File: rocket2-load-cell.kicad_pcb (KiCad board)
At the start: 2 copper layers, 45.1 x 100.6 mm, 41 parts, among them J1 SWD, J2 Screw_Terminal_01x02, J3 629105150521, U1 STM32F103C8Tx, U2 AMS1117-3.3, Y1 16MHz

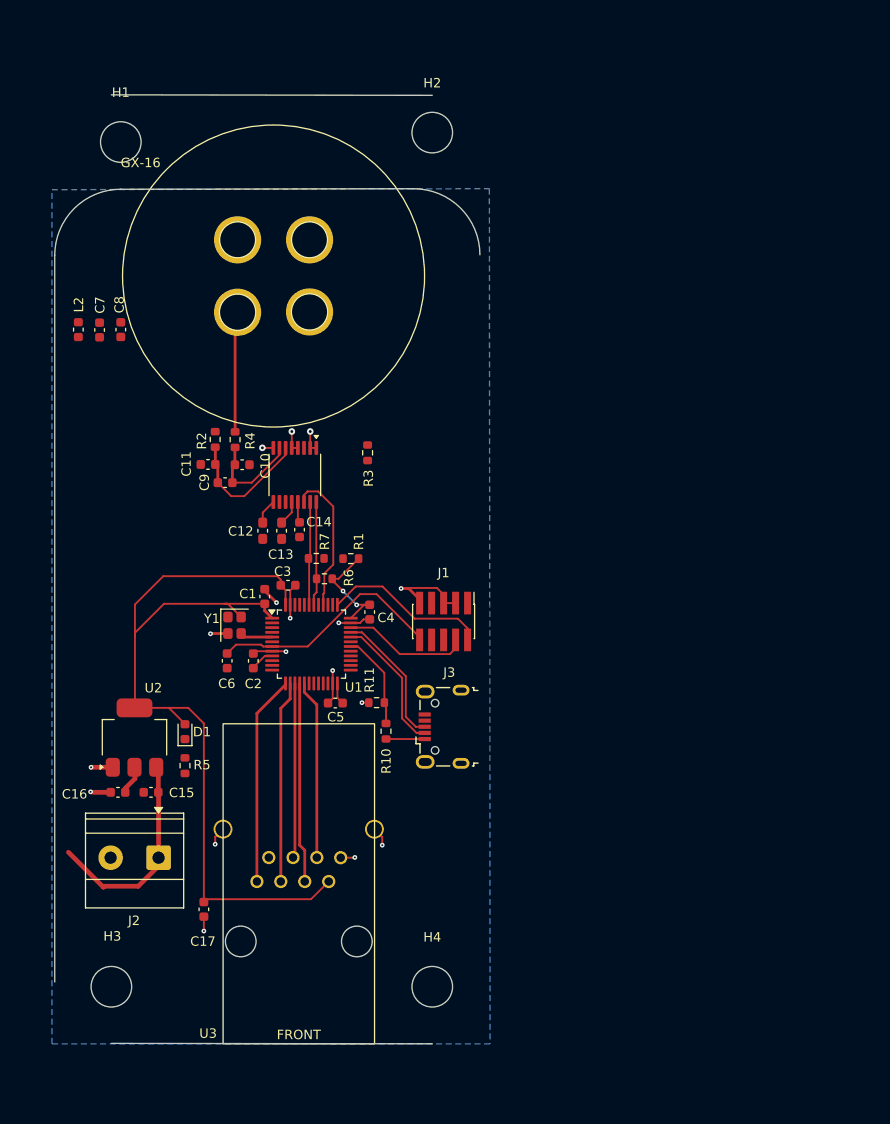
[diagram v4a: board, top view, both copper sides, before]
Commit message: complete power + signal routing
fixed bends, shortened length from MCU -> ADC -> Load Cell
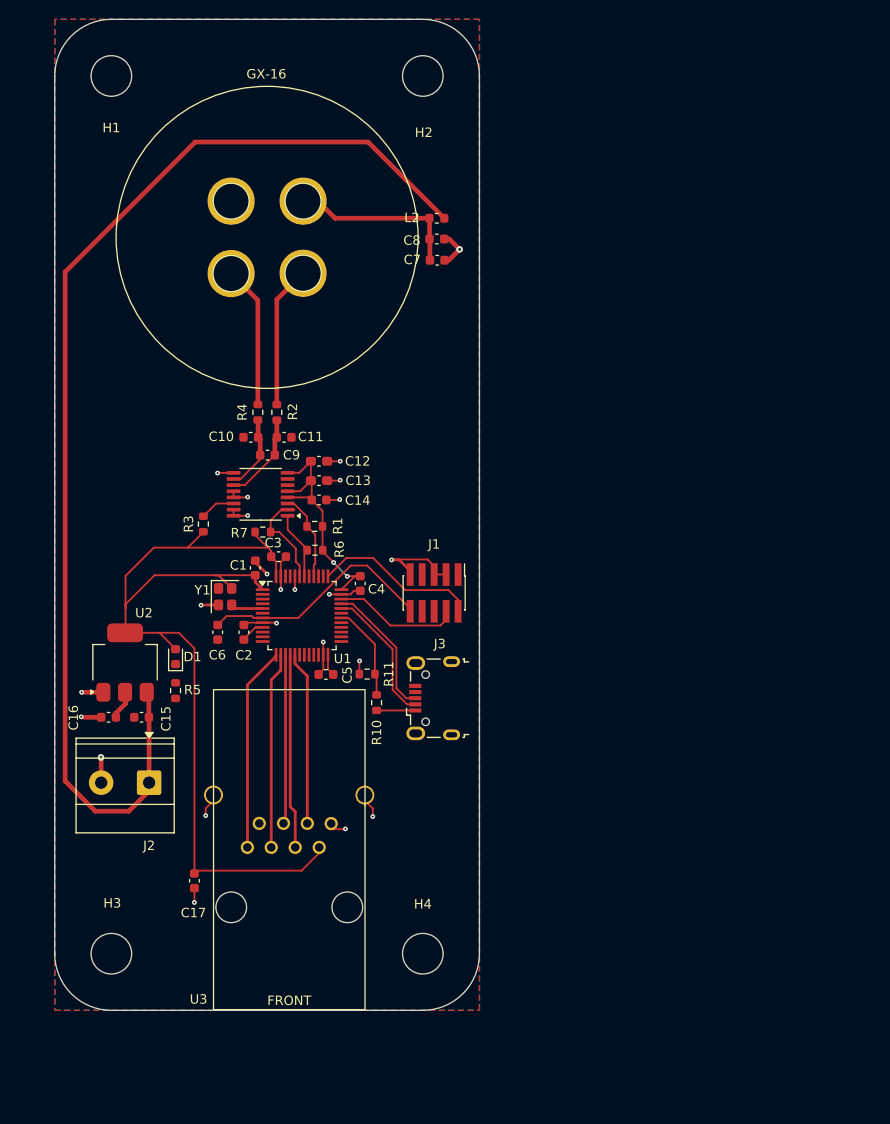
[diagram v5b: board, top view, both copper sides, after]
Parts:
- moved L2 39.8 mm to (150.5, 56.1), turned to 0 degrees
- moved C7 36.5 mm to (150.5, 60.5), turned to 0 degrees
- moved C8 34.8 mm to (150.5, 58.3), turned to 0 degrees
- moved R3 19.0 mm to (125.8, 88.5)
- moved C12 9.48 mm to (138.0, 81.8), turned to 0 degrees
- moved C11 8.57 mm to (134.3, 79.3), turned to 180 degrees
- moved C15 8.01 mm to (119.2, 109.0)
- moved C16 8.01 mm to (115.7, 109.0)
- moved J2 8.01 mm to (120.0, 115.9)
- moved R5 8.01 mm to (122.8, 106.1)
- moved D1 8.01 mm to (122.8, 102.5)
- moved U2 8.01 mm to (117.5, 103.2)
- moved R2 7.13 mm to (133.5, 76.6)
- moved H1 7.07 mm to (116.0, 41.0)
- moved C13 6.63 mm to (138.0, 83.9), turned to 0 degrees
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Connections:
- ADS1219 pad 1: GND -> ADS_CLK
- ADS1219 pad 10: unconnected-(ADS1219-AIN1-Pad10) -> Net-(ADS1219-AIN1)
- ADS1219 pad 11: unconnected-(ADS1219-AIN0-Pad11) -> Net-(ADS1219-AIN0)
- ADS1219 pad 12: +3.3V -> GND
- ADS1219 pad 13: +3.3V -> GND
- ADS1219 pad 14: ADS_DRDY -> Net-(ADS1219-DRDY)
- ADS1219 pad 15: ADS_DATA -> GND
- ADS1219 pad 16: ADS_CLK -> GND
- ADS1219 pad 2: GND -> ADS_DATA
- ADS1219 pad 3: Net-(ADS1219-RESET) -> ADS_DRDY
- ADS1219 pad 4: GND -> +3.3V
- ADS1219 pad 5: GND -> +3.3V
- ADS1219 pad 6: Net-(ADS1219-AIN3) -> unconnected-(ADS1219-AIN3-Pad6)
- ADS1219 pad 7: Net-(ADS1219-AIN2) -> unconnected-(ADS1219-AIN2-Pad7)
- ADS1219 pad 8: GND -> +3.3V
- ADS1219 pad 9: +3.3V -> GND
- C10 pad 2: Net-(ADS1219-AIN2) -> Net-(ADS1219-AIN1)
- C11 pad 2: Net-(ADS1219-AIN3) -> Net-(ADS1219-AIN0)
- C9 pad 1: Net-(ADS1219-AIN3) -> Net-(ADS1219-AIN0)
- C9 pad 2: Net-(ADS1219-AIN2) -> Net-(ADS1219-AIN1)
- R2 pad 2: Net-(ADS1219-AIN3) -> Net-(ADS1219-AIN0)
- R3 pad 1: Net-(ADS1219-RESET) -> Net-(ADS1219-DRDY)
- R4 pad 2: Net-(ADS1219-AIN2) -> Net-(ADS1219-AIN1)
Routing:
- net VBUS: track 22.6 -> 124.8 mm
- net VLC: track 0.00 -> 18.6 mm
- net AIN-: track 0.00 -> 15.1 mm
- net Net-(ADS1219-AIN3): track 14.2 -> 0.00 mm
- net GND: track 47.0 -> 60.6 mm, vias 17 -> 23
- net +3.3V: track 120.9 -> 132.8 mm
- net Net-(ADS1219-AIN2): track 10.8 -> 0.00 mm
- net Net-(ADS1219-AIN0): track 0.00 -> 9.80 mm
- net Net-(ADS1219-AIN1): track 0.00 -> 7.94 mm
- net ADS_DRDY: track 15.5 -> 9.37 mm
- net Net-(ADS1219-DRDY): track 0.00 -> 3.76 mm
- net ADS_CLK: track 11.0 -> 7.33 mm
- net AIN+: track 12.8 -> 15.0 mm
- net ETH_RX: track 21.2 -> 20.6 mm
- net ETH_RTS: track 21.4 -> 20.8 mm
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- added copper zone on F.Cu, net GND
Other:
- board size 45.1 x 100.6 mm -> 45 x 105 mm

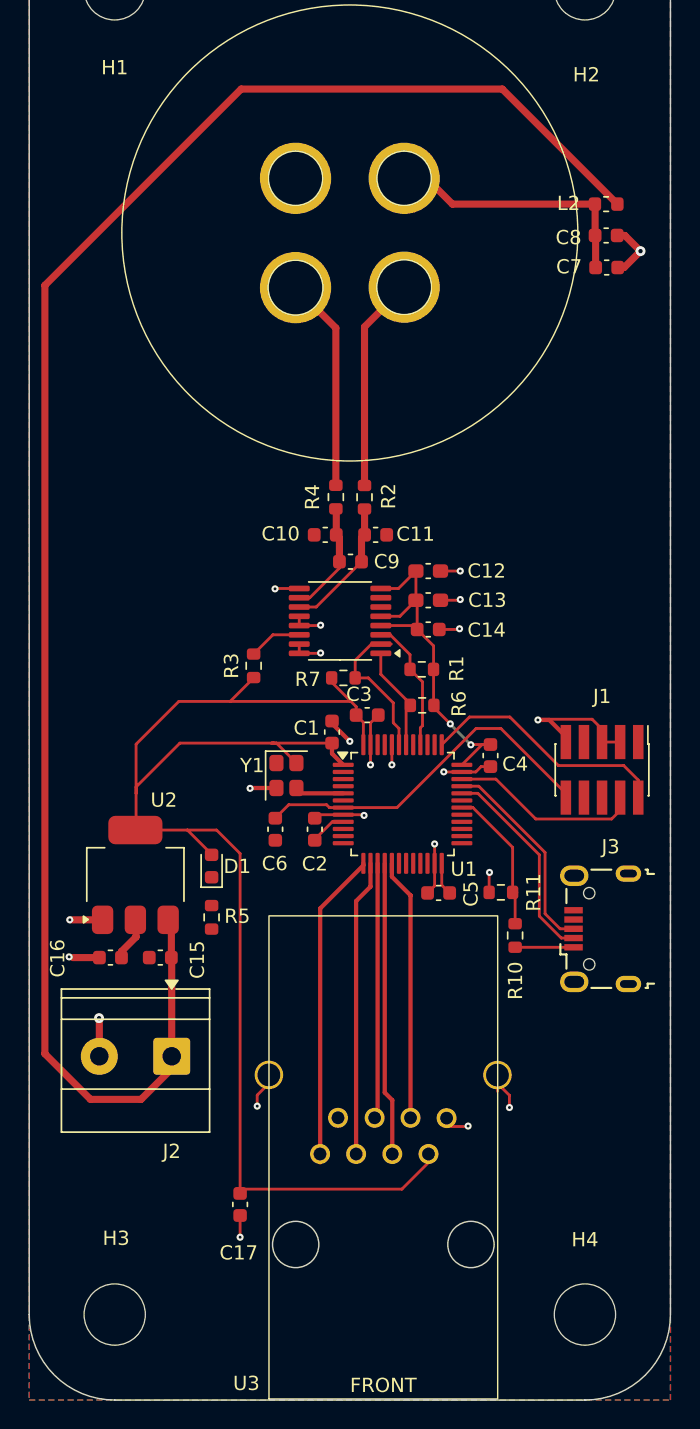
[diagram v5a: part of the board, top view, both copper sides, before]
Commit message: Barrel Jack, New Regulator, and Full Routing
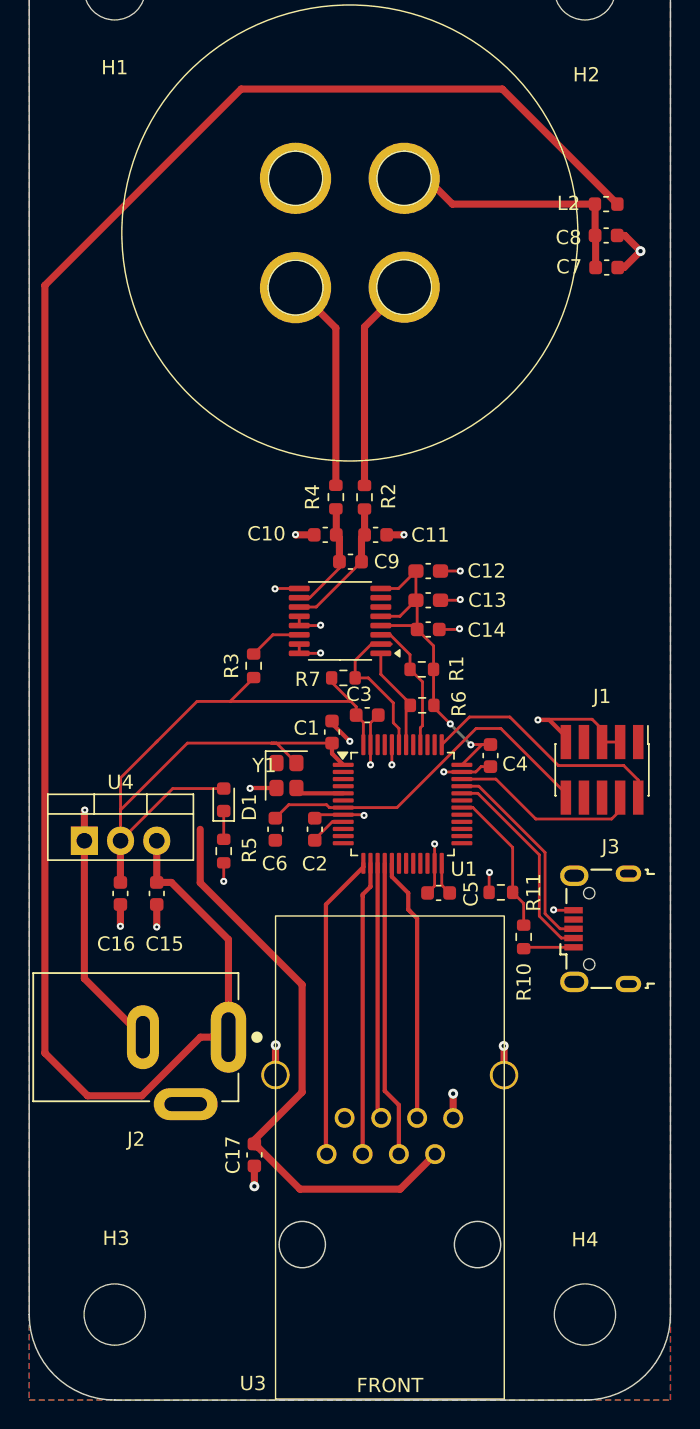
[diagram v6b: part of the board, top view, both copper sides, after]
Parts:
- removed U2: AMS1117-3.3, Package_TO_SOT_SMD:SOT-223-3_TabPin2
- added U4: LD1117V33, Package_TO_SOT_THT:TO-220-3_Vertical, F.Cu at (113.9, 100.8)
- C15: value 22uF -> 100nF
- C16: value 22uF -> 10uF
- J2: value Screw_Terminal_01x02 -> PJ-002A; footprint TerminalBlock_Phoenix:TerminalBlock_Phoenix_MKDS-1,5-2-5.08_1x02_P5.08mm_Horizontal -> UCIRP-KiCAD-Lib:CUI_PJ-202A
- moved D1 4.73 mm to (123.7, 97.9)
- moved R5 4.73 mm to (123.7, 101.5)
- moved C16 4.55 mm to (116.4, 104.5), turned to 90 degrees
- moved C15 4.51 mm to (119.0, 104.5), turned to 90 degrees
- moved C17 3.61 mm to (125.8, 122.8)
- moved J2 2.85 mm to (117.5, 114.5)
- moved R10 0.61 mm to (144.7, 107.5)
- moved U3 0.46 mm to (135.3, 123.0)
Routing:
- net GND: track 60.6 -> 79.8 mm, vias 23 -> 27
- net VBUS: track 124.8 -> 136.2 mm
- net +3.3V: track 132.8 -> 139.1 mm
- net Net-(D1-K): track 0.00 -> 1.99 mm
- net ETH_CTS: track 22.2 -> 21.5 mm
- net USB_VBUS: track 4.10 -> 3.54 mm
- net Net-(U1-PA9): track 10.4 -> 11.0 mm

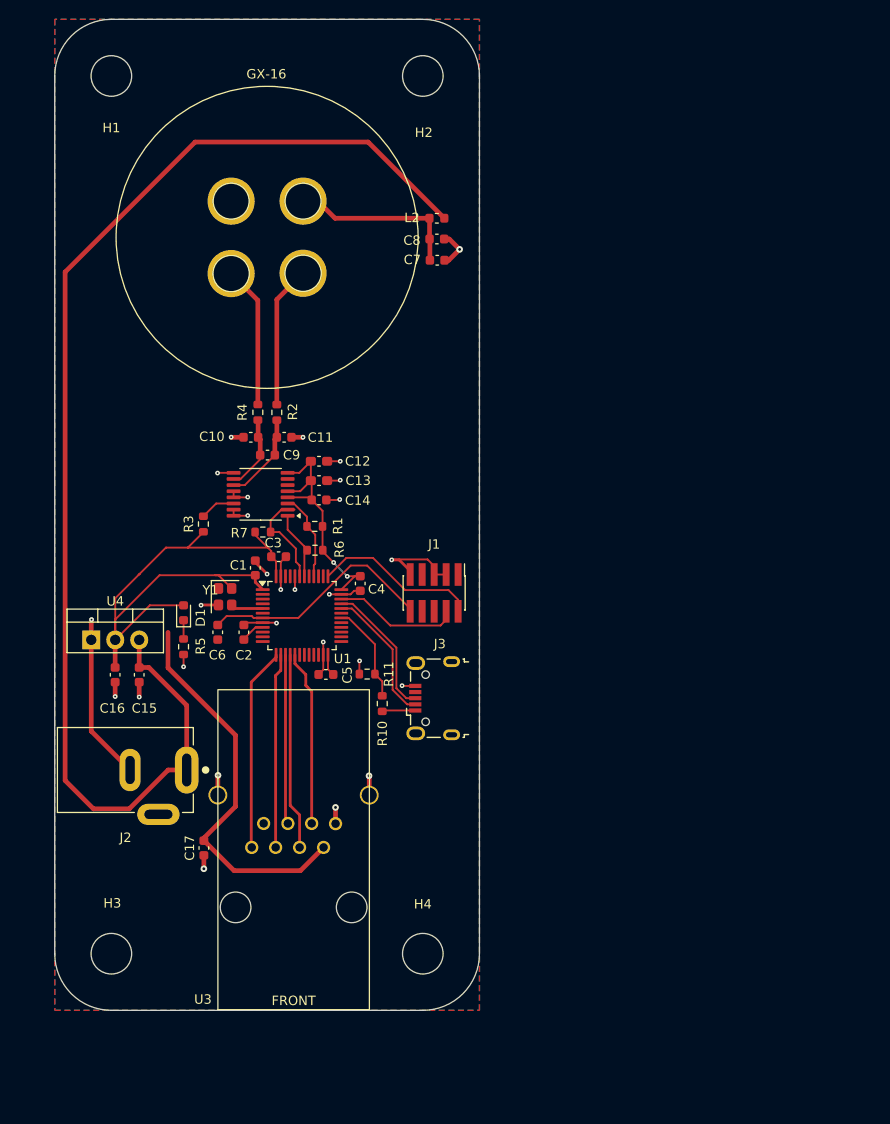
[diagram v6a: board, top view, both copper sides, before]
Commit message: Updated based on DRC
Filled zones filled
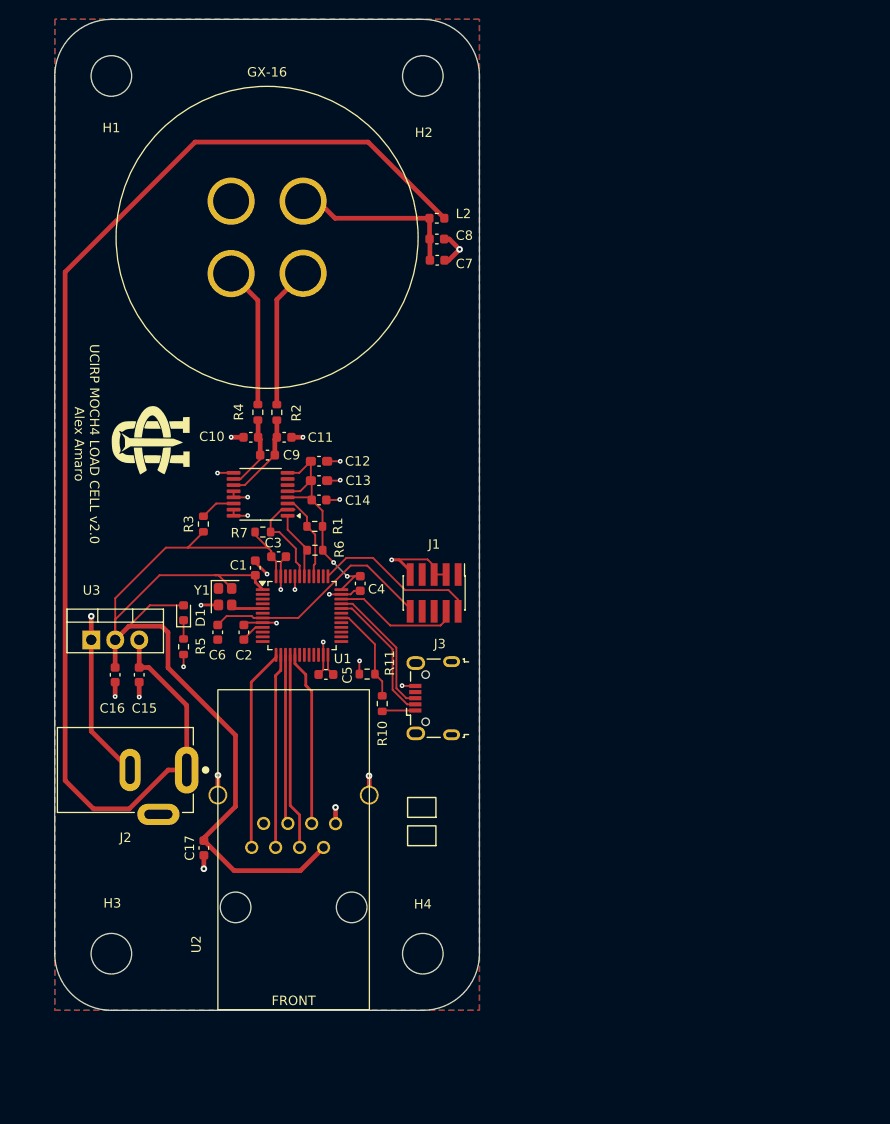
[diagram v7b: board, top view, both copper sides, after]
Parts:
- added G***: LOGO, UCILIB:uci_rocket_logo, F.Cu at (120.2, 79.6)
- C9: value 0.1uF -> 100nF
- GX-16: value ~ -> J1
- R2, R4: value 330 -> 1k
- renumbered U3 to U2, U4 to U3
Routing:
- net +3.3V: track 139.1 -> 145.4 mm
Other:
- board text added: "UCIRP MOCH4 LOAD CELL v2.0 Alex Amaro"
- board text added: "千空"

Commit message: Added Through-hole Backup Power
Redundancy for the barrel jack
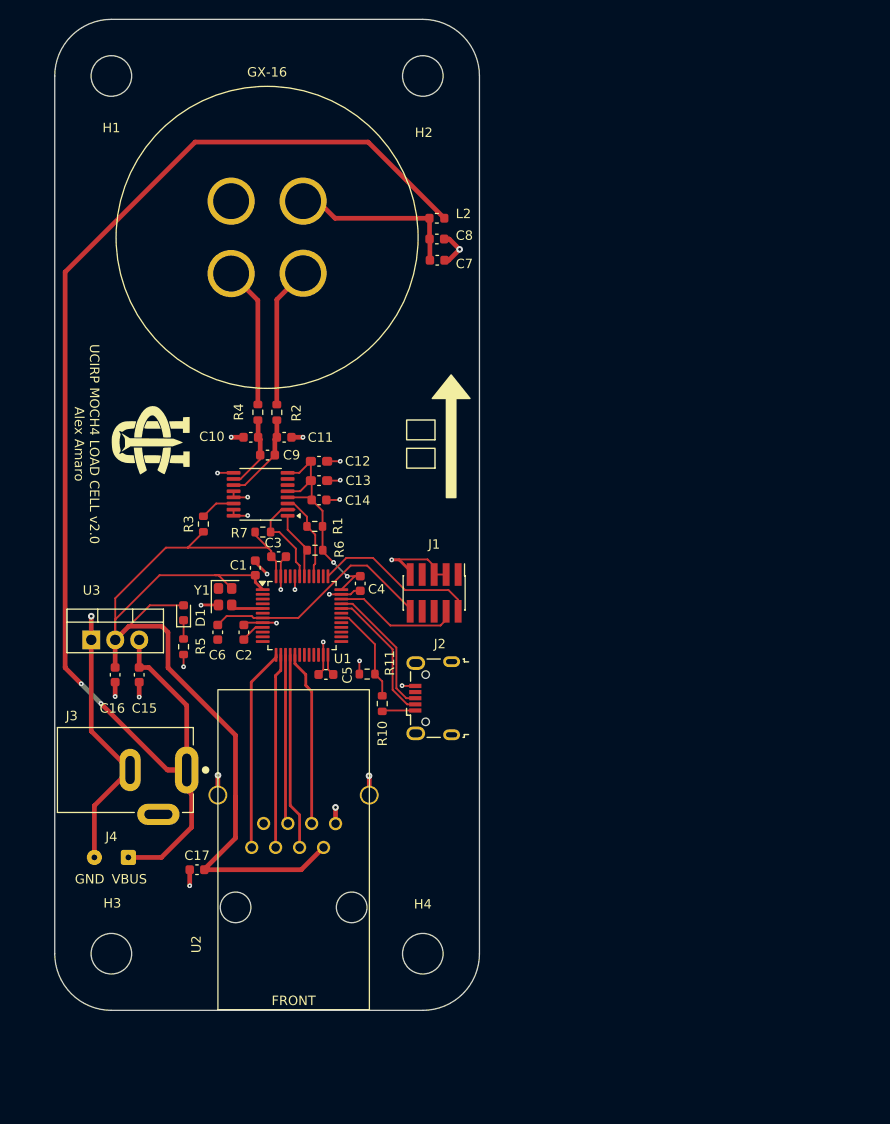
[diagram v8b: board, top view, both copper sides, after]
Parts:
- added J4: Conn_01x02, Connector_Wire:SolderWire-0.1sqmm_1x02_P3.6mm_D0.4mm_OD1mm, F.Cu at (117.8, 123.8)
- moved C17 2.41 mm to (125.1, 125.1), turned to 180 degrees
- renumbered J3 to J2, J2 to J3
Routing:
- net GND: track 80.2 -> 91.3 mm
- net VBUS: track 136.2 -> 142.1 mm, vias 0 -> 2
- net +3.3V: track 145.4 -> 147.9 mm
- removed copper zone on B.Cu, net GND
- removed copper zone on F.Cu, net GND
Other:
- board text added: "GND"
- board text added: "VBUS"
